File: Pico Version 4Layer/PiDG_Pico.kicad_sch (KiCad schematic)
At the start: 67 parts, among them J1 Conn_02x05_Odd_Even, J10 Trig, J11 Laser Enable, J12 Pixel Reset, J14 Pico Socket A, J15 Pico Socket B, J16 Laser En/PWM Trig/GND, J17 USB-C PD in, J2 Conn_02x05_Odd_Even, J3 Conn_02x05_Odd_Even, J4 Conn_02x05_Odd_Even, J5 Conn_02x05_Odd_Even, J6 Conn_02x05_Odd_Even, J7 Laser 1, J8 Laser 2, U1 74LVC1G04, U10 74AHCT1G08, U11 Raspberry Pi Pico 2 W, U12 74LVC1G17, U13 UCC27524, U14 CH224K, U15 AP63205WU, U16 LM66100, U17 LP2951D, U2 SN74LVC04AD, U3 74LVC1G04, U4 SN74LVC04AD, U5 74LVC1G04, U6 SN74LVC04AD, U7 74AHCT1G08, U8 74AHCT1G08, U9 NCP718xSN180

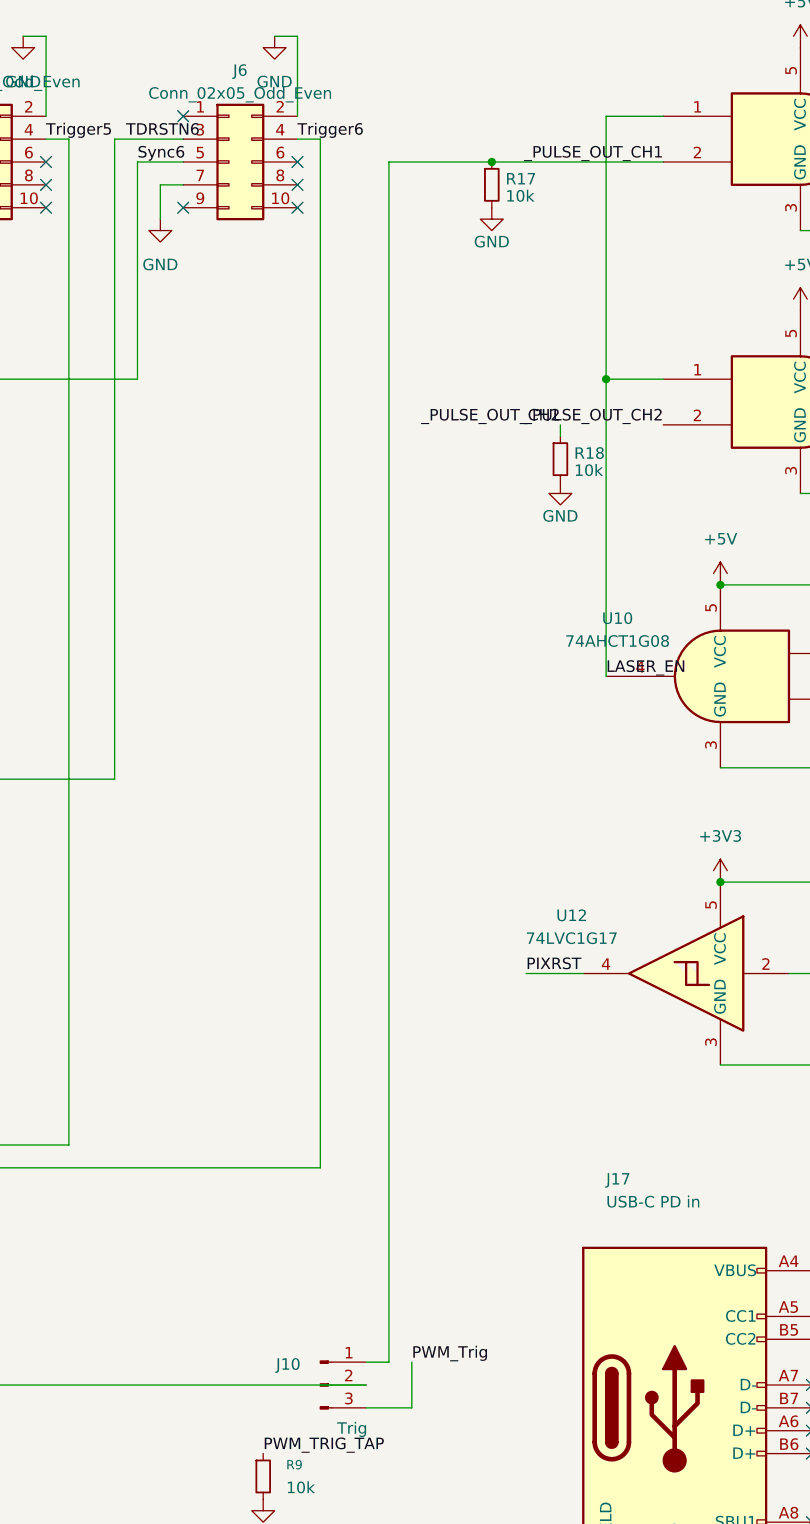
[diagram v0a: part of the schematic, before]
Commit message: Final DFM/SI review: layout fixes, fresh fab outputs, JLC files, README
Board (Pico Version 4Layer), from a fab / assembly / signal-integrity review:
- U13 decoupling: C9 (0.1 uF 50 V) moved beside VDD pin 6 with its own GND
  via; GND pin 3 gets a direct plane via; +12V via moved under the package;
  R6/R7 shifted 2 mm out to make room. Loop ~1.5-2 nH, was 7-13 nH.
- R19 100 ohm in series with J10 pin 1 (new net CH1_J10): with J10 on 1-2,
  the PWM_TRIG_TAP load made CH1 arrive 0.4-1.7 ns after CH2.
- No vias left inside SMD pads except U14's exposed-pad thermal vias:
  13 moved off their pads (U13 ENA/ENB now joined on F.Cu), 9 nudged clear
  of neighbouring mask openings.
- 47 edge stitching vias and 7 local GND vias at decoupling caps / IC grounds.
- 3 mm copper keep-out around each M3 hole; zone-to-edge clearance 0.5 mm.
- Silkscreen: TP3 reference restored ("1MHz Clock" kept as board text),
  J10 relabelled CH1/TRG/MKR, J11 ON/OFF, Pico outline + USB-end arrow +
  pin-1 mark, references moved off vias.
- U11 (socketed Pico) marked not-on-board / not-in-BOM in the schematic.
DRC 0 violations / 0 unconnected, ERC 0, all 334 pads match the schematic.

Outputs: gerbers, drills and zip regenerated (the previous set predated the
silkscreen edits); BOM/CPL updated (R19, capacitor voltage/dielectric,
loose jumper shunts); fab/jlc/ holds JLC-format SMD BOM and CPL with the
LCSC column left for part selection.

Docs: new top-level README (quick start, connecting, full command reference
with replies captured from the firmware, troubleshooting, wireless as a
future option); tools/pidg_example.py; Hardware.md gains manufacturing notes
and first-power-up checks and loses stale claims (finest pitch, RUN button,
TX_DROPPED unit, J16 interlock, Wi-Fi range).

Co-Authored-By: Claude Opus 5.5 (1M context) <noreply@anthropic.com>
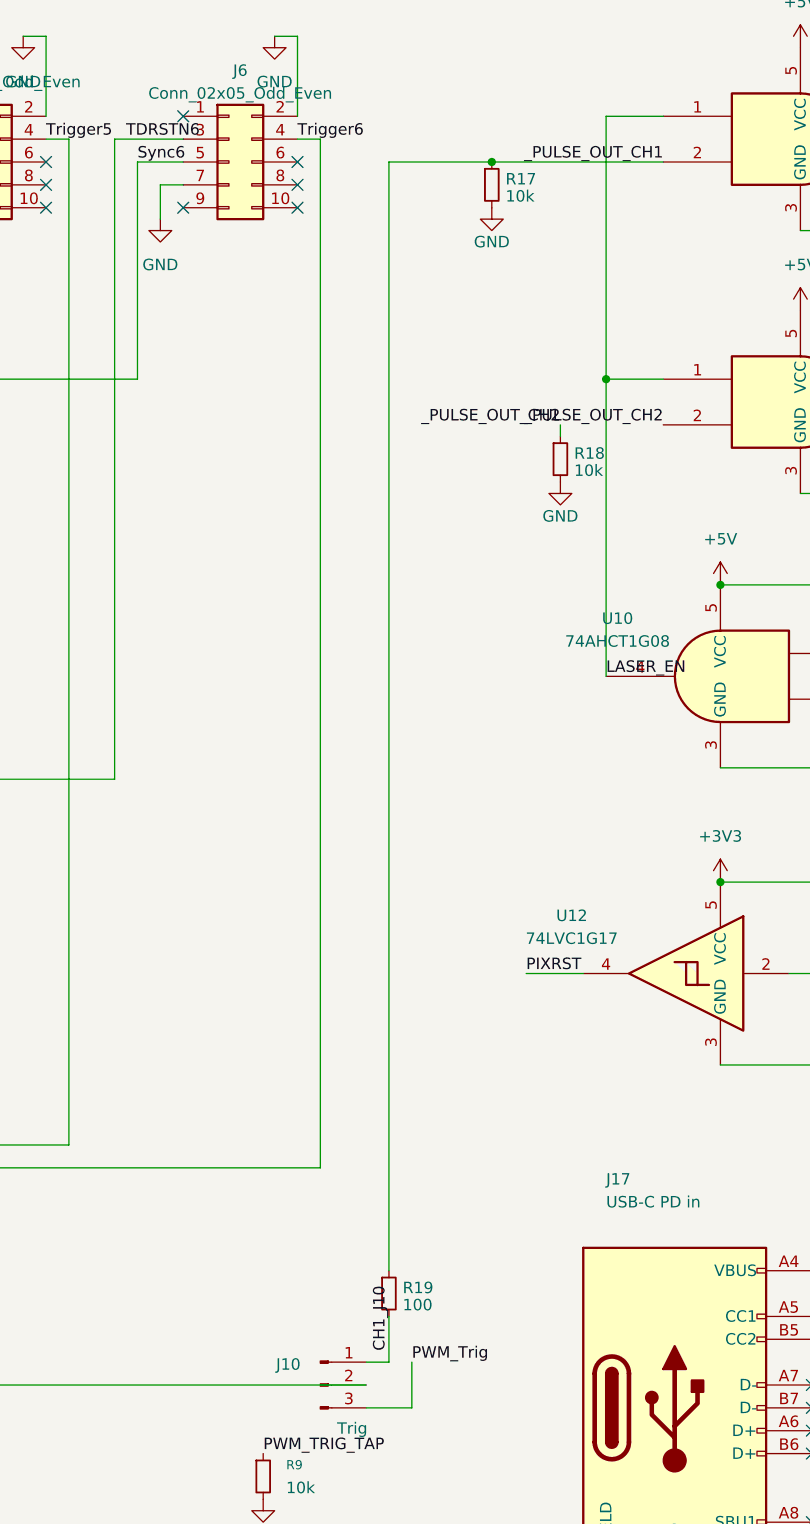
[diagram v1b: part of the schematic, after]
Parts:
- added R19: 100, Resistor_SMD:R_0805_2012Metric_Pad1.20x1.40mm_HandSolder, symbol Device:R_Small
- U11: now left out of the parts list
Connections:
- net _PULSE_OUT_CH1: now also R19.1; no longer J10.1 (Pin_1)
- new net CH1_J10: J10.1 (Pin_1), R19.2
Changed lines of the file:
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@@
 	(wire
 		(pts
-			(xy 293.37 31.75) (xy 293.37 165.1)
+			(xy 293.37 31.75) (xy 293.37 154.94)
+		)
+		(stroke
+			(width 0)
+			(type default)
+		)
+	)
+	(wire
+		(pts
+			(xy 293.37 160.02) (xy 293.37 165.1)
 		)
 		(stroke
@@
 		)
 	)
+	(label "CH1_J10"
+		(at 293.37 163.83 90)
+		(effects
+			(font
+				(size 1.27 1.27)
+			)
+			(justify left bottom)
+		)
+	)
 	(label "PWM_TRIG_TAP"
 		(at 279.4 175.26 0)
@@
 		(body_style 1)
 		(exclude_from_sim no)
-		(in_bom yes)
-		(on_board yes)
-		(in_pos_files yes)
+		(in_bom no)
+		(on_board no)
+		(in_pos_files no)
 		(dnp no)
 		(fields_autoplaced yes)
@@
 					(unit 1)
 				)
+			)
+		)
+	)
+	(symbol
+		(lib_id "Device:R_Small")
+		(at 293.37 157.48 0)
+		(unit 1)
+		(body_style 1)
+		(exclude_from_sim no)
+		(in_bom yes)
+		(on_board yes)
+		(in_pos_files yes)
+		(dnp no)
+		(property "Reference" "R19"
+			(at 294.894 156.845 0)
+			(show_name no)
+			(do_not_autoplace no)
+			(effects
+				(font
+					(size 1.27 1.27)
+				)
+				(justify left)
+			)
+		)
+		(property "Value" "100"
+			(at 294.894 158.75 0)
+			(show_name no)
+			(do_not_autoplace no)
+			(effects
+				(font
+					(size 1.27 1.27)
+				)
+				(justify left)
+			)
+		)
+		(property "Footprint" "Resistor_SMD:R_0805_2012Metric_Pad1.20x1.40mm_HandSolder"
+			(at 293.37 157.48 0)
+			(hide yes)
+			(show_name no)
+			(do_not_autoplace no)
+			(effects
+				(font
+					(size 1.27 1.27)
+				)
+			)
+		)
+		(property "Datasheet" ""
+			(at 293.37 157.48 0)
+			(hide yes)
+			(show_name no)
+			(do_not_autoplace no)
+			(effects
+				(font
+					(size 1.27 1.27)
+				)
+			)
+		)
+		(property "Description" "Series isolation for J10 pin 1: keeps the PWM_TRIG_TAP load (J10 on 1-2) off the CH1 laser pulse edge"
+			(at 293.37 157.48 0)
+			(hide yes)
+			(show_name no)
+			(do_not_autoplace no)
+			(effects
+				(font
+					(size 1.27 1.27)
+				)
+			)
+		)
+		(pin "1"
+		)
+		(pin "2"
+		)
+		(instances
+			(project "PiDG_Pico"
+				(path "/e63e39d7-6ac0-4ffd-8aa3-1841a4541b55"
+					(reference "R19")
+					(unit 1)
+				)

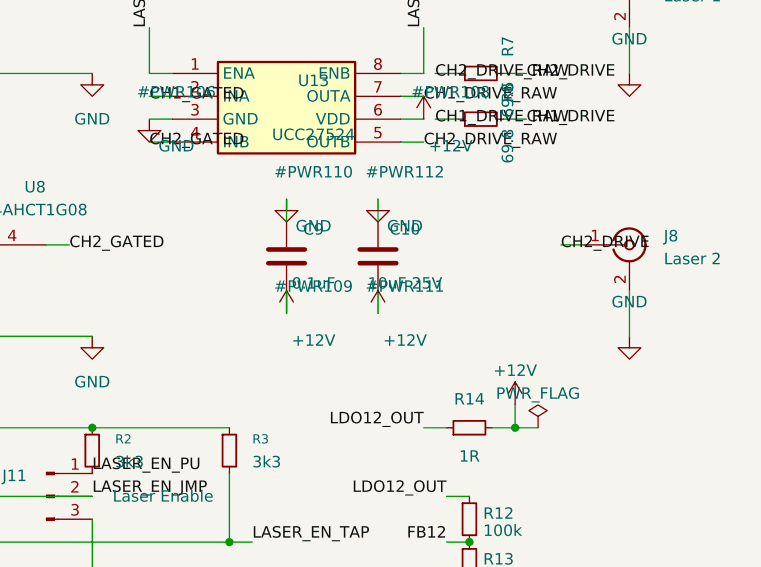
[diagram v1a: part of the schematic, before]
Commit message: JLC full-assembly order package: LCSC numbers for all 67 parts, THT in CPL, checklist
- fab/jlc/PiDG_Pico_JLC_BOM.csv: 34 lines, every one with an LCSC number
  checked against JLC's library (2026-09-25); through-hole connectors and
  headers included so JLC fits everything.
- fab/jlc/PiDG_Pico_JLC_CPL.csv: all 67 parts; through-hole parts at their
  pad centre (footprint origins are on pin 1).
- fab/jlc/JLC_ORDER.md: order-form settings, remarks, parts needing Global
  Sourcing (CH224K and NCP718 out of stock; 69.8R stock thin), rotation
  checks, cost estimate, on-delivery steps and enclosure notes.
- C6/C11 -> 1 uF 50 V (shares C16's basic part), C10 -> 10 uF 50 V (shares
  C12's part): two fewer extended-part fees. Human BOM gains an LCSC column.
- Back silkscreen: JLC order-number placeholder. Gerbers/drills/zip
  regenerated; DRC 0/0, ERC 0.

Co-Authored-By: Claude Opus 5.5 (1M context) <noreply@anthropic.com>
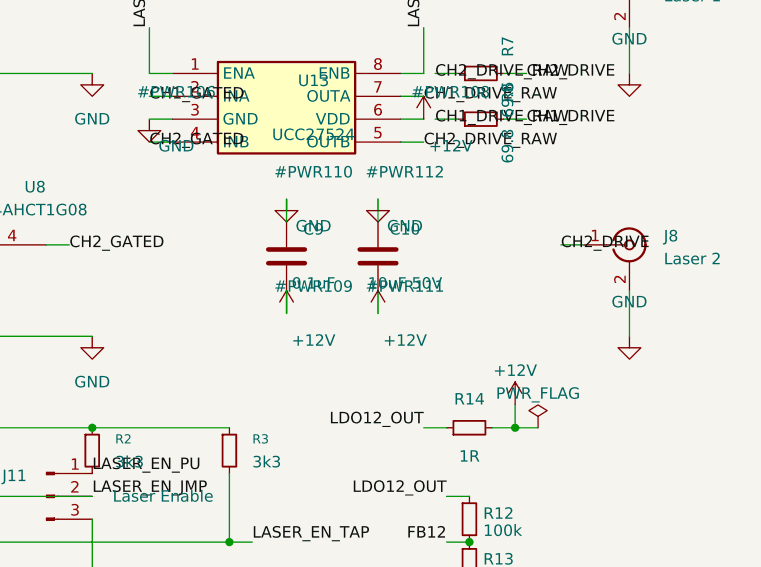
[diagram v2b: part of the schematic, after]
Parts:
- C10: value 10uF 25V -> 10uF 50V
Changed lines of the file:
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@@
 			)
 		)
-		(property "Value" "10uF 25V"
+		(property "Value" "10uF 50V"
 			(at 391.62 62.69 0)
 			(show_name no)

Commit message: 12 V rail and laser output resistors upgraded: no board duty limit
The laser outputs were limited by the board itself: R6/R7 were 0.125 W 0805
(<= ~19 % duty into 50 ohm) and the LP2951 12 V regulator was rated 100 mA
(both outputs high need ~200 mA). Now the board carries any duty the
firmware accepts, even into a shorted BNC.

- U17 LP2951 SOIC-8 -> LT3065EDD (adjustable, 45 V / 500 mA, DFN-10):
  R12/R13 101k/5.36k 0.1 % -> 11.9 V (11.65-12.17 V worst case), R20 750R
  sets a 400 mA current limit, C18 22 nF on IMAX, C19 10 nF on BYP, C17
  10 uF output cap. R14 (the LP2951's ESR resistor) removed.
- New U18 TPS3700 window comparator (R21/R22/R23 1M/6.04k/31.6k, C20)
  drives LASER_PWR_OK: U13 stays disabled unless +12V is inside
  11.0-13.1 V, which also catches a failed-short regulator.
- R6/R7 69.8R 0805 -> 68R 1 % 2 W 2512. Amplitude into 50 ohm
  4.61-5.08 V (typ 4.84 V), inside the LDP-V's 4.5-5.2 V window.
- Board: U17 cluster rebuilt around (219, 76.5), U18 cluster in the free
  pocket left of the +12V trunk, VBUS_PD fed on B.Cu, R6/R7 re-placed.
  DRC 0 / 0 unconnected, ERC 0, schematic parity equal to the baseline.
- Gerbers, drill, zip, CPL and BOMs (human + JLC, 40 lines / 75 parts,
  all in stock except the already-flagged U9/U14) regenerated;
  README, Hardware.md and JLC_ORDER.md updated.

Co-Authored-By: Claude Opus 5.5 (1M context) <noreply@anthropic.com>
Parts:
- removed R14: 1R, Resistor_SMD:R_0805_2012Metric_Pad1.20x1.40mm_HandSolder, symbol Device:R_Small
- added C17: 10uF 50V, Capacitor_SMD:C_1206_3216Metric_Pad1.33x1.80mm_HandSolder, symbol Device:C
- added C18: 22nF, Capacitor_SMD:C_0805_2012Metric_Pad1.18x1.45mm_HandSolder, symbol Device:C
- added C19: 10nF, Capacitor_SMD:C_0805_2012Metric_Pad1.18x1.45mm_HandSolder, symbol Device:C
- added C20: 0.1uF, Capacitor_SMD:C_0805_2012Metric_Pad1.18x1.45mm_HandSolder, symbol Device:C
- added R20: 750, Resistor_SMD:R_0805_2012Metric_Pad1.20x1.40mm_HandSolder, symbol Device:R_Small
- added R21: 1M, Resistor_SMD:R_0805_2012Metric_Pad1.20x1.40mm_HandSolder, symbol Device:R_Small
- added R22: 6.04k, Resistor_SMD:R_0805_2012Metric_Pad1.20x1.40mm_HandSolder, symbol Device:R_Small
- added R23: 31.6k, Resistor_SMD:R_0805_2012Metric_Pad1.20x1.40mm_HandSolder, symbol Device:R_Small
- added U18: TPS3700DDC, Package_TO_SOT_SMD:SOT-23-6, symbol PiDG_Local:TPS3700DDC
- R12: value 100k -> 101k
- R13: value 11.3k -> 5.36k
- R6, R7: value 69.8 -> 68; footprint Resistor_SMD:R_0805_2012Metric_Pad1.20x1.40mm_HandSolder -> Resistor_SMD:R_2512_6332Metric_Pad1.40x3.35mm_HandSolder
- U17: value LP2951D -> LT3065EDD; footprint Package_SO:SOIC-8_3.9x4.9mm_P1.27mm -> Package_DFN_QFN:DFN-10-1EP_3x3mm_P0.5mm_EP1.65x2.38mm; symbol Regulator_Linear:LP2951-3.0_SOIC -> PiDG_Local:LT3065xDD
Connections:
- net +12V: now also R12.1, U17.10 (OUT), U17.9 (OUT), C17.1, C20.1, R21.1, U18.5 (VDD)
- net GND: now also U17.11 (EP), U17.7 (GND), C17.2, C18.2, C19.2, C20.2, R20.2, R23.2, U18.2 (GND); no longer U17.3 (SHUTDOWN), U17.4 (GND)
- net LASER_PWR_OK: now also U18.1 (OUTA), U18.6 (OUTB); no longer U17.5 (~{ERROR})
- net VBUS_PD: now also U17.1 (IN), U17.2 (IN), U17.3 (SHDN); no longer U17.8 (IN)
- net at U17.6 (BYP): now also C19.1
- net FB12: no longer names the net of R12.2, R13.1
- net FB12: now also U17.8 (ADJ); no longer U17.7 (FEEDBACK)
- removed net LDO12_OUT: R12.1, U17.1 (OUT)
- new net: R21.2, R22.1, U18.3 (INA+)
- new net: R22.2, R23.1, U18.4 (INB-)
- new net: C18.1, R20.1, U17.5 (IMAX)
- no-connect marks 96 -> 95
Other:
- note added: "U17: 11.9 V laser rail, 400 mA limit (R20). U18 (sheet bottom left) holds U13 disabled (LASER_PWR_OK low) unless +12V is inside 11.0-13.1 V (TPS3700 window)."
- note added: "USB-C PD input. U14 requests 15 V. U15 buck + U16 ideal diode feed the +5V plane (Pico VSYS). U17 makes the 11.9 V +12V rail for U13; U18 gates U13's enables (see the note by U17). Pico VBUS is NOT on +5V: USB reaches VSYS only through the Pico's own Schottky."
- note removed: "USB-C PD input. U14 requests 15 V. U15 buck + U16 ideal diode feed the +5V plane (Pico VSYS). U17 makes 12.0 V for U13 and holds U13 disabled (LASER_PWR_OK low) until it is in regulation. Pico VBUS is NOT on +5V: USB reaches VSYS only through the Pico's own Schottky."
- moved on the sheet: C16, R12, R13
